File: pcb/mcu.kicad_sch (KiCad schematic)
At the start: 33 parts, among them CN9 2x5, IC2 STM32f103C8T

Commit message: added DIP switches, footprints
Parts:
- removed TP6, TP7, TP8: test_point, PCB:test_point, symbol PCB:test_point
- renumbered TP9 to TP6, TP10 to TP7, TP11 to TP8
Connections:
- net ADDR1: now reaches IC2.21 (PB10)
- net ADDR2: now reaches IC2.22 (PB11)
- net ADDR3: now reaches IC2.25 (PB12)
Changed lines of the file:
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@@
+    (stroke (width 0) (type default))
+  )
+  (wire (pts (xy 160.02 124.46) (xy 162.56 124.46))
     (stroke (width 0) (type default))
   )
@@
     (stroke (width 0) (type default))
   )
+  (wire (pts (xy 160.02 121.92) (xy 162.56 121.92))
+    (stroke (width 0) (type default))
+  )
   (wire (pts (xy 198.12 86.36) (xy 198.12 88.9))
     (stroke (width 0) (type default))
@@
   )
   (wire (pts (xy 116.84 91.44) (xy 127 91.44))
+    (stroke (width 0) (type default))
+  )
+  (wire (pts (xy 160.02 127) (xy 162.56 127))
     (stroke (width 0) (type default))
   )
@@
     (effects (font (size 1.27 1.27)) (justify right))
   )
+  (hierarchical_label "ADDR2" (shape input) (at 162.56 124.46 0) (fields_autoplaced)
+    (effects (font (size 1.27 1.27)) (justify left))
+  )
   (hierarchical_label "CH6" (shape output) (at 132.08 114.3 180) (fields_autoplaced)
     (effects (font (size 1.27 1.27)) (justify right))
@@
     (effects (font (size 1.27 1.27)) (justify left))
   )
+  (hierarchical_label "ADDR1" (shape input) (at 162.56 121.92 0) (fields_autoplaced)
+    (effects (font (size 1.27 1.27)) (justify left))
+  )
   (hierarchical_label "I_bat" (shape input) (at 132.08 99.06 180) (fields_autoplaced)
     (effects (font (size 1.27 1.27)) (justify right))
   )
+  (hierarchical_label "ADDR3" (shape input) (at 162.56 127 0) (fields_autoplaced)
+    (effects (font (size 1.27 1.27)) (justify left))
+  )
   (hierarchical_label "CH4" (shape output) (at 132.08 104.14 180) (fields_autoplaced)
     (effects (font (size 1.27 1.27)) (justify right))
   )
-  (symbol (lib_id "PCB:test_point") (at 160.02 121.92 0) (unit 1)
-    (in_bom yes) (on_board yes) (dnp no) (fields_autoplaced)
-    (property "Reference" "TP6" (at 163.83 121.6025 0)
-      (effects (font (size 1.27 1.27)) (justify left))
-    )
-    (property "Value" "test_point" (at 160.02 119.38 0)
-      (effects (font (size 1.27 1.27)) hide)
-    )
-    (property "Footprint" "PCB:test_point" (at 162.56 123.19 0)
-      (effects (font (size 1.27 1.27)) hide)
-    )
-    (property "Datasheet" "" (at 160.02 121.92 0)
-      (effects (font (size 1.27 1.27)) hide)
-    )
-    (pin "1")
-    (instances
-      (project "pcb"
-        (path "/6bb3bad6-1a89-4624-b34d-6ddda7dd16d2/19469851-aeaf-466c-9786-c0d0ae531cf4"
-          (reference "TP6") (unit 1)
-        )
-      )
-    )
-  )
   (symbol (lib_name "xtal_gnd_1") (lib_id "generic:xtal_gnd") (at 182.88 78.74 0) (unit 1)
     (in_bom yes) (on_board yes) (dnp no)
@@
         (path "/6bb3bad6-1a89-4624-b34d-6ddda7dd16d2/19469851-aeaf-466c-9786-c0d0ae531cf4"
           (reference "C18") (unit 1)
-        )
-      )
-    )
-  )
-  (symbol (lib_id "PCB:test_point") (at 160.02 124.46 0) (unit 1)
-    (in_bom yes) (on_board yes) (dnp no) (fields_autoplaced)
-    (property "Reference" "TP7" (at 163.83 124.1425 0)
-      (effects (font (size 1.27 1.27)) (justify left))
-    )
-    (property "Value" "test_point" (at 160.02 121.92 0)
-      (effects (font (size 1.27 1.27)) hide)
-    )
-    (property "Footprint" "PCB:test_point" (at 162.56 125.73 0)
-      (effects (font (size 1.27 1.27)) hide)
-    )
-    (property "Datasheet" "" (at 160.02 124.46 0)
-      (effects (font (size 1.27 1.27)) hide)
-    )
-    (pin "1")
-    (instances
-      (project "pcb"
-        (path "/6bb3bad6-1a89-4624-b34d-6ddda7dd16d2/19469851-aeaf-466c-9786-c0d0ae531cf4"
-          (reference "TP7") (unit 1)
         )
       )
@@
     )
   )
-  (symbol (lib_id "PCB:test_point") (at 160.02 127 0) (unit 1)
-    (in_bom yes) (on_board yes) (dnp no) (fields_autoplaced)
-    (property "Reference" "TP8" (at 163.83 126.6825 0)
-      (effects (font (size 1.27 1.27)) (justify left))
-    )
-    (property "Value" "test_point" (at 160.02 124.46 0)
-      (effects (font (size 1.27 1.27)) hide)
-    )
-    (property "Footprint" "PCB:test_point" (at 162.56 128.27 0)
-      (effects (font (size 1.27 1.27)) hide)
-    )
-    (property "Datasheet" "" (at 160.02 127 0)
-      (effects (font (size 1.27 1.27)) hide)
-    )
-    (pin "1")
-    (instances
-      (project "pcb"
-        (path "/6bb3bad6-1a89-4624-b34d-6ddda7dd16d2/19469851-aeaf-466c-9786-c0d0ae531cf4"
-          (reference "TP8") (unit 1)
-        )
-      )
-    )
-  )
   (symbol (lib_id "generic:C") (at 177.8 81.28 0) (mirror y) (unit 1)
     (in_bom yes) (on_board yes) (dnp no)
@@
   (symbol (lib_id "PCB:test_point") (at 160.02 132.08 0) (unit 1)
     (in_bom yes) (on_board yes) (dnp no) (fields_autoplaced)
-    (property "Reference" "TP10" (at 163.83 131.7625 0)
+    (property "Reference" "TP7" (at 163.83 131.7625 0)
       (effects (font (size 1.27 1.27)) (justify left))
     )
@@
       (project "pcb"
         (path "/6bb3bad6-1a89-4624-b34d-6ddda7dd16d2/19469851-aeaf-466c-9786-c0d0ae531cf4"
-          (reference "TP10") (unit 1)
+          (reference "TP7") (unit 1)
         )
       )
@@
   (symbol (lib_id "PCB:test_point") (at 160.02 134.62 0) (unit 1)
     (in_bom yes) (on_board yes) (dnp no) (fields_autoplaced)
-    (property "Reference" "TP11" (at 163.83 134.3025 0)
+    (property "Reference" "TP8" (at 163.83 134.3025 0)
       (effects (font (size 1.27 1.27)) (justify left))
     )
@@
       (project "pcb"
         (path "/6bb3bad6-1a89-4624-b34d-6ddda7dd16d2/19469851-aeaf-466c-9786-c0d0ae531cf4"
-          (reference "TP11") (unit 1)
+          (reference "TP8") (unit 1)
         )
       )
@@
   (symbol (lib_id "PCB:test_point") (at 160.02 129.54 0) (unit 1)
     (in_bom yes) (on_board yes) (dnp no) (fields_autoplaced)
-    (property "Reference" "TP9" (at 163.83 129.2225 0)
+    (property "Reference" "TP6" (at 163.83 129.2225 0)
       (effects (font (size 1.27 1.27)) (justify left))
     )
@@
       (project "pcb"
         (path "/6bb3bad6-1a89-4624-b34d-6ddda7dd16d2/19469851-aeaf-466c-9786-c0d0ae531cf4"
-          (reference "TP9") (unit 1)
-        )
-      )
+          (reference "TP6") (unit 1)
+        )
+      )

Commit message: updated components. worked on layout
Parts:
- removed C3, C?: 100n, SMT:0603, symbol generic:C
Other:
- moved on the sheet: C?

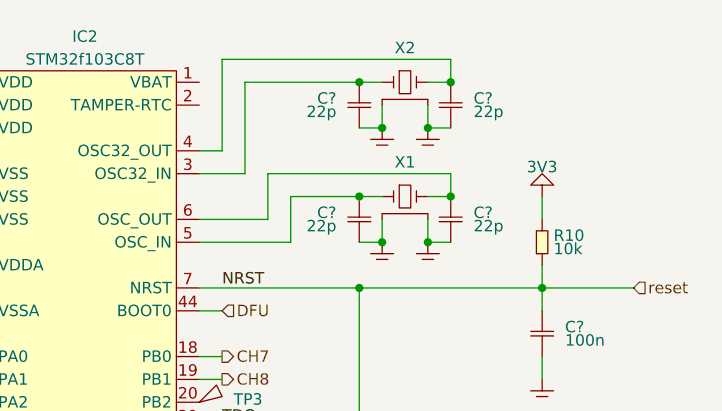
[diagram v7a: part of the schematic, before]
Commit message: added missing footprints
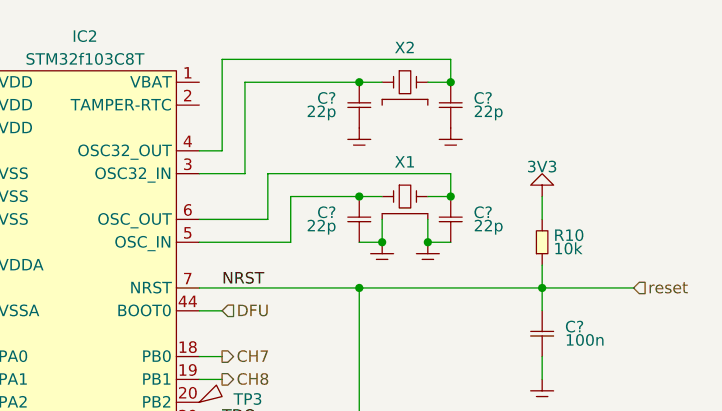
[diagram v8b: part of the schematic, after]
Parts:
- X1: value ~ -> H130B-8.000-18-3030-EXT-TR; footprint (none) -> xtal:5x3.2; DigiKey (none) -> 2151-H130B-8.000-18-3030-EXT-TRCT-ND; MPN (none) -> H130B-8.000-18-3030-EXT-TR
- X2: value ~ -> 32.768K12.5PI/MC306; footprint (none) -> xtal:8x3.2; symbol generic:xtal_gnd -> oscillators:32.768K12.5PI/MC306; DigiKey (none) -> 3155-32.768K12.5PI/MC306CT-ND; MPN (none) -> 32.768K12.5PI/MC306
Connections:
- net GND: no longer X2.2, X2.4
- net at C?.1, IC2.4 (OSC32_OUT): now also X2.4; no longer X2.3
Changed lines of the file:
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@@
   (junction (at 104.14 134.62) (diameter 0) (color 0 0 0 0)
   )
-  (junction (at 185.42 71.12) (diameter 0) (color 0 0 0 0)
-  )
   (junction (at 180.34 83.82) (diameter 0) (color 0 0 0 0)
   )
@@
   (junction (at 177.8 66.04) (diameter 0) (color 0 0 0 0)
   )
-  (junction (at 180.34 71.12) (diameter 0) (color 0 0 0 0)
-  )
   (junction (at 127 86.36) (diameter 0) (color 0 0 0 0)
   )
@@
     (stroke (width 0) (type default))
   )
-  (wire (pts (xy 177.8 71.12) (xy 180.34 71.12))
-    (stroke (width 0) (type default))
-  )
   (wire (pts (xy 104.14 139.7) (xy 106.68 139.7))
     (stroke (width 0) (type default))
@@
     (stroke (width 0) (type default))
   )
-  (wire (pts (xy 185.42 71.12) (xy 187.96 71.12))
-    (stroke (width 0) (type default))
-  )
   (wire (pts (xy 129.54 137.16) (xy 129.54 134.62))
     (stroke (width 0) (type default))
@@
     (stroke (width 0) (type default))
   )
-  (wire (pts (xy 185.42 68.58) (xy 185.42 71.12))
-    (stroke (width 0) (type default))
-  )
   (wire (pts (xy 104.14 132.08) (xy 104.14 134.62))
     (stroke (width 0) (type default))
@@
   )
   (wire (pts (xy 132.08 111.76) (xy 134.62 111.76))
-    (stroke (width 0) (type default))
-  )
-  (wire (pts (xy 180.34 68.58) (xy 180.34 71.12))
     (stroke (width 0) (type default))
   )
@@
       (effects (font (size 1.27 1.27)))
     )
-    (property "Value" "~" (at 182.88 78.74 0)
-      (effects (font (size 1.27 1.27)))
-    )
-    (property "Footprint" "" (at 182.88 78.74 0)
-      (effects (font (size 1.27 1.27)) hide)
-    )
-    (property "Datasheet" "" (at 182.88 78.74 0)
+    (property "Value" "H130B-8.000-18-3030-EXT-TR" (at 182.88 78.74 0)
+      (effects (font (size 1.27 1.27)) hide)
+    )
+    (property "Footprint" "xtal:5x3.2" (at 182.88 78.74 0)
+      (effects (font (size 1.27 1.27)) hide)
+    )
+    (property "Datasheet" "https://www.raltron.com/webproducts/specs/CRYSTAL/CKP/H130B-8.000-18-3030-EXT-TR.pdf" (at 182.88 78.74 0)
+      (effects (font (size 1.27 1.27)) hide)
+    )
+    (property "MPN" "H130B-8.000-18-3030-EXT-TR" (at 182.88 78.74 0)
+      (effects (font (size 1.27 1.27)) hide)
+    )
+    (property "DigiKey" "2151-H130B-8.000-18-3030-EXT-TRCT-ND" (at 182.88 78.74 0)
       (effects (font (size 1.27 1.27)) hide)
     )
@@
     )
   )
-  (symbol (lib_id "generic:xtal_gnd") (at 182.88 66.04 0) (unit 1)
+  (symbol (lib_id "oscillators:32.768K12.5PI/MC306") (at 182.88 66.04 0) (unit 1)
     (in_bom yes) (on_board yes) (dnp no)
     (property "Reference" "X2" (at 182.88 62.23 0)
       (effects (font (size 1.27 1.27)))
     )
-    (property "Value" "~" (at 182.88 66.04 0)
-      (effects (font (size 1.27 1.27)))
-    )
-    (property "Footprint" "" (at 182.88 66.04 0)
-      (effects (font (size 1.27 1.27)) hide)
-    )
-    (property "Datasheet" "" (at 182.88 66.04 0)
+    (property "Value" "32.768K12.5PI/MC306" (at 182.88 66.04 0)
+      (effects (font (size 1.27 1.27)) hide)
+    )
+    (property "Footprint" "xtal:8x3.2" (at 182.88 49.53 0)
+      (effects (font (size 1.27 1.27)) hide)
+    )
+    (property "Datasheet" "https://www.yic.com.tw/wp-content/uploads/2023/11/YIC-MC306-Series.pdf" (at 182.88 57.15 0)
+      (effects (font (size 1.27 1.27)) hide)
+    )
+    (property "MPN" "32.768K12.5PI/MC306" (at 182.88 52.07 0)
+      (effects (font (size 1.27 1.27)) hide)
+    )
+    (property "DigiKey" "3155-32.768K12.5PI/MC306CT-ND" (at 182.88 54.61 0)
       (effects (font (size 1.27 1.27)) hide)
     )
@@
     )
   )
-  (symbol (lib_id "generic:GND") (at 185.42 71.12 0) (unit 1)
-    (in_bom yes) (on_board yes) (dnp no) (fields_autoplaced)
-    (property "Reference" "#GND025" (at 189.23 69.85 0)
-      (effects (font (size 1.27 1.27)) hide)
-    )
-    (property "Value" "GND" (at 189.23 71.12 0)
-      (effects (font (size 1.27 1.27)) hide)
-    )
-    (property "Footprint" "" (at 185.42 71.12 0)
-      (effects (font (size 1.27 1.27)) hide)
-    )
-    (property "Datasheet" "" (at 185.42 71.12 0)
+  (symbol (lib_id "generic:GND") (at 187.96 71.12 0) (unit 1)
+    (in_bom yes) (on_board yes) (dnp no) (fields_autoplaced)
+    (property "Reference" "#GND025" (at 191.77 69.85 0)
+      (effects (font (size 1.27 1.27)) hide)
+    )
+    (property "Value" "GND" (at 191.77 71.12 0)
+      (effects (font (size 1.27 1.27)) hide)
+    )
+    (property "Footprint" "" (at 187.96 71.12 0)
+      (effects (font (size 1.27 1.27)) hide)
+    )
+    (property "Datasheet" "" (at 187.96 71.12 0)
       (effects (font (size 1.27 1.27)) hide)
     )
@@
     )
   )
-  (symbol (lib_id "generic:GND") (at 180.34 71.12 0) (unit 1)
-    (in_bom yes) (on_board yes) (dnp no) (fields_autoplaced)
-    (property "Reference" "#GND024" (at 184.15 69.85 0)
-      (effects (font (size 1.27 1.27)) hide)
-    )
-    (property "Value" "GND" (at 184.15 71.12 0)
-      (effects (font (size 1.27 1.27)) hide)
-    )
-    (property "Footprint" "" (at 180.34 71.12 0)
-      (effects (font (size 1.27 1.27)) hide)
-    )
-    (property "Datasheet" "" (at 180.34 71.12 0)
-      (effects (font (size 1.27 1.27)) hide)
-    )
+  (symbol (lib_id "generic:GND") (at 177.8 71.12 0) (unit 1)
+    (in_bom yes) (on_board yes) (dnp no) (fields_autoplaced)
+    (property "Reference" "#GND024" (at 181.61 69.85 0)
+      (effects (font (size 1.27 1.27)) hide)
+    )
+    (property "Value" "GND" (at 181.61 71.12 0)
+      (effects (font (size 1.27 1.27)) hide)
+    )
+    (property "Footprint" "" (at 177.8 71.12 0)
+      (effects (font (size 1.27 1.27)) hide)
+    )
+    (property "Datasheet" "" (at 177.8 71.12 0)
+      (effects (font (size 1.27 1.27)) hide)
+    )
